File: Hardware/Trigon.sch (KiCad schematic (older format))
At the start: 110 parts, among them J1 TYPE-C-31-M12_13, J2 TYPE-C-31-M12_13, J3 Conn_01x05, SW1 SW_Push, SW2 Rotary_Encoder_Switch, U1 ATmega32U4-AU, U2 USBLC6-2SC6, U3 CY7C65632-28LTXCT, U4 USBLC6-2SC6, Y1 16MHz, Y2 12MHz

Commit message: crystal load
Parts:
- C12, C13, C14, C17, C18, C21, C4, C5, C6, C8: Manufacturer Part # CC0805KRX7R9BB104 -> CC0603KRX7R9BB104
- C19, C20: Manufacturer Part # (none) -> CC0603KRX7R9BB104
- Y1: Manufacturer Part # X322516MLB4SI -> X322516MOB4SI
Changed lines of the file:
@@
 F 2 "Capacitor_SMD:C_0603_1608Metric" H 4700 3200 50  0001 C CNN
 F 3 "~" H 4700 3200 50  0001 C CNN
-F 4 "CC0805KRX7R9BB104" H 4700 3200 50  0001 C CNN "Manufacturer Part #"
+F 4 "CC0603KRX7R9BB104" H 4700 3200 50  0001 C CNN "Manufacturer Part #"
 	1    4700 3200
 	1    0    0    -1
@@
 F 2 "Capacitor_SMD:C_0603_1608Metric" H 5000 3200 50  0001 C CNN
 F 3 "~" H 5000 3200 50  0001 C CNN
-F 4 "CC0805KRX7R9BB104" H 5000 3200 50  0001 C CNN "Manufacturer Part #"
+F 4 "CC0603KRX7R9BB104" H 5000 3200 50  0001 C CNN "Manufacturer Part #"
 	1    5000 3200
 	1    0    0    -1
@@
 F 2 "Capacitor_SMD:C_0603_1608Metric" H 5300 3200 50  0001 C CNN
 F 3 "~" H 5300 3200 50  0001 C CNN
-F 4 "CC0805KRX7R9BB104" H 5300 3200 50  0001 C CNN "Manufacturer Part #"
+F 4 "CC0603KRX7R9BB104" H 5300 3200 50  0001 C CNN "Manufacturer Part #"
 	1    5300 3200
 	1    0    0    -1
@@
 F 2 "Capacitor_SMD:C_0603_1608Metric" H 10450 13900 50  0001 C CNN
 F 3 "~" H 10450 13900 50  0001 C CNN
-F 4 "CC0805KRX7R9BB104" H 10450 13900 50  0001 C CNN "Manufacturer Part #"
+F 4 "CC0603KRX7R9BB104" H 10450 13900 50  0001 C CNN "Manufacturer Part #"
 	1    10450 13900
 	1    0    0    -1
@@
 F 2 "Capacitor_SMD:C_0603_1608Metric" H 11500 13800 50  0001 C CNN
 F 3 "~" H 11500 13800 50  0001 C CNN
-F 4 "CC0805KRX7R9BB104" H 11500 13800 50  0001 C CNN "Manufacturer Part #"
+F 4 "CC0603KRX7R9BB104" H 11500 13800 50  0001 C CNN "Manufacturer Part #"
 	1    11500 13800
 	1    0    0    -1
@@
 F 2 "Capacitor_SMD:C_0603_1608Metric" H 11950 13800 50  0001 C CNN
 F 3 "~" H 11950 13800 50  0001 C CNN
-F 4 "CC0805KRX7R9BB104" H 11950 13800 50  0001 C CNN "Manufacturer Part #"
+F 4 "CC0603KRX7R9BB104" H 11950 13800 50  0001 C CNN "Manufacturer Part #"
 	1    11950 13800
 	1    0    0    -1
@@
 F 2 "Capacitor_SMD:C_0603_1608Metric" H 13300 13800 50  0001 C CNN
 F 3 "~" H 13300 13800 50  0001 C CNN
-F 4 "CC0805KRX7R9BB104" H 13300 13800 50  0001 C CNN "Manufacturer Part #"
+F 4 "CC0603KRX7R9BB104" H 13300 13800 50  0001 C CNN "Manufacturer Part #"
 	1    13300 13800
 	1    0    0    -1
@@
 F 2 "Capacitor_SMD:C_0603_1608Metric" H 8350 10200 50  0001 C CNN
 F 3 "~" H 8350 10200 50  0001 C CNN
-F 4 "CC0805KRX7R9BB104" H 8350 10200 50  0001 C CNN "Manufacturer Part #"
+F 4 "CC0603KRX7R9BB104" H 8350 10200 50  0001 C CNN "Manufacturer Part #"
 	1    8350 10200
 	1    0    0    -1
@@
 F 2 "Capacitor_SMD:C_0603_1608Metric" H 19750 7350 50  0001 C CNN
 F 3 "~" H 19750 7350 50  0001 C CNN
-F 4 "CC0805KRX7R9BB104" H 19750 7350 50  0001 C CNN "Manufacturer Part #"
+F 4 "CC0603KRX7R9BB104" H 19750 7350 50  0001 C CNN "Manufacturer Part #"
 	1    19750 7350
 	1    0    0    -1
@@
 F 2 "Crystal:Crystal_SMD_3225-4Pin_3.2x2.5mm" H 1750 2350 50  0001 C CNN
 F 3 "~" H 1750 2350 50  0001 C CNN
-F 4 "X322516MLB4SI" H 1750 2350 50  0001 C CNN "Manufacturer Part #"
+F 4 "X322516MOB4SI" H 1750 2350 50  0001 C CNN "Manufacturer Part #"
 	1    1750 2350
 	0    1    1    0
@@
 F 2 "Capacitor_SMD:C_0603_1608Metric" H 1500 10400 50  0001 C CNN
 F 3 "~" H 1500 10400 50  0001 C CNN
+F 4 "CC0603KRX7R9BB104" H 1500 10400 50  0001 C CNN "Manufacturer Part #"
 	1    1500 10400
 	1    0    0    -1
@@
 F 2 "Capacitor_SMD:C_0603_1608Metric" H 18300 10350 50  0001 C CNN
 F 3 "~" H 18300 10350 50  0001 C CNN
+F 4 "CC0603KRX7R9BB104" H 18300 10350 50  0001 C CNN "Manufacturer Part #"
 	1    18300 10350
 	1    0    0    -1
@@
 F 2 "Capacitor_SMD:C_0603_1608Metric" H 3300 7450 50  0001 C CNN
 F 3 "~" H 3300 7450 50  0001 C CNN
-F 4 "CC0805KRX7R9BB104" H 3300 7450 50  0001 C CNN "Manufacturer Part #"
+F 4 "CC0603KRX7R9BB104" H 3300 7450 50  0001 C CNN "Manufacturer Part #"
 	1    3300 7450
 	1    0    0    -1

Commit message: Gerbers
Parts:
- J3: Manufacturer Part # (none) -> SM05B-SRSS-TB(LF)(SN)
- R15, R16: Manufacturer Part # (none) -> 0603WAF1003T5E
- U2, U4: Manufacturer Part # (none) -> USBLC6-2SC6
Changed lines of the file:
@@
 F 2 "Resistor_SMD:R_0603_1608Metric" H 1250 10400 50  0001 C CNN
 F 3 "~" H 1250 10400 50  0001 C CNN
+F 4 "0603WAF1003T5E" H 1250 10400 50  0001 C CNN "Manufacturer Part #"
 	1    1250 10400
 	1    0    0    -1
@@
 F 2 "Resistor_SMD:R_0603_1608Metric" H 18050 10350 50  0001 C CNN
 F 3 "~" H 18050 10350 50  0001 C CNN
+F 4 "0603WAF1003T5E" H 18050 10350 50  0001 C CNN "Manufacturer Part #"
 	1    18050 10350
 	1    0    0    -1
@@
 F 2 "Package_TO_SOT_SMD:SOT-23-6" H 2850 9650 50  0001 C CNN
 F 3 "http://www2.st.com/resource/en/datasheet/CD00050750.pdf" H 3800 9600 50  0001 C CNN
+F 4 "USBLC6-2SC6" H 3600 9250 50  0001 C CNN "Manufacturer Part #"
 	1    3600 9250
 	1    0    0    -1
@@
 F 2 "Package_TO_SOT_SMD:SOT-23-6" H 20150 9550 50  0001 C CNN
 F 3 "http://www2.st.com/resource/en/datasheet/CD00050750.pdf" H 21100 9500 50  0001 C CNN
+F 4 "USBLC6-2SC6" H 20900 9150 50  0001 C CNN "Manufacturer Part #"
 	1    20900 9150
 	1    0    0    -1
@@
 F 2 "Connector_JST:JST_SH_SM05B-SRSS-TB_1x05-1MP_P1.00mm_Horizontal" H 19650 12900 50  0001 C CNN
 F 3 "~" H 19650 12900 50  0001 C CNN
+F 4 "SM05B-SRSS-TB(LF)(SN)" H 19650 12900 50  0001 C CNN "Manufacturer Part #"
 	1    19650 12900
 	1    0    0    -1

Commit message: New layout
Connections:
- net +3V3: now also FB1.1, U3.21 (VCC_D); no longer C8.1, FB1.2
- new net: C8.1, FB1.2
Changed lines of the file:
@@
 Text GLabel 9400 13650 0    50   Input ~ 0
 VREG_3V3
-$Comp
-L power:+3.3V #PWR0132
-U 1 1 5F992A63
-P 9850 13550
-F 0 "#PWR0132" H 9850 13400 50  0001 C CNN
-F 1 "+3.3V" H 9865 13723 50  0000 C CNN
-F 2 "" H 9850 13550 50  0001 C CNN
-F 3 "" H 9850 13550 50  0001 C CNN
-	1    9850 13550
-	1    0    0    -1
-$EndComp
 Wire Wire Line
 	9400 13650 9650 13650
-Wire Wire Line
-	9850 13650 9850 13550
 $Comp
 L Device:C_Small C12
@@
 $EndComp
 Wire Wire Line
-	9850 13650 10050 13650
-Connection ~ 9850 13650
+	9650 13650 10050 13650
 $Comp
 L power:+3.3VA #PWR0133
@@
 	9650 13800 9650 13650
 Connection ~ 9650 13650
-Wire Wire Line
-	9650 13650 9850 13650
 $Comp
 L power:GND #PWR0134
@@
 $EndComp
 Wire Wire Line
-	8350 10100 8350 10050
-Wire Wire Line
 	8350 10300 8350 10400
 NoConn ~ 19200 7600
@@
 Wire Wire Line
 	2300 2800 2300 2850
-$Comp
-L power:+3.3V #PWR0122
-U 1 1 5F430011
-P 8250 10050
-F 0 "#PWR0122" H 8250 9900 50  0001 C CNN
-F 1 "+3.3V" V 8265 10178 50  0000 L CNN
-F 2 "" H 8250 10050 50  0001 C CNN
-F 3 "" H 8250 10050 50  0001 C CNN
-	1    8250 10050
-	0    -1   -1   0
-$EndComp
-Wire Wire Line
-	8250 10050 8350 10050
-Wire Wire Line
-	10150 9750 10850 9750
+Wire Wire Line
+	10150 9750 10350 9750
 Wire Wire Line
 	9950 9750 8350 9750
-Wire Wire Line
-	8350 9750 8350 10050
-Connection ~ 8350 10050
 Wire Wire Line
 	3800 7250 4200 7250
@@
 	1    0    0    -1
 $EndComp
+Wire Wire Line
+	8350 9750 8350 10100
+Wire Wire Line
+	10350 9700 10350 9750
+Connection ~ 10350 9750
+Wire Wire Line
+	10350 9750 10850 9750
+Wire Wire Line
+	9650 13450 9650 13650
+$Comp
+L power:+3.3V #PWR?
+U 1 1 5F5BCA3D
+P 9650 13450
+F 0 "#PWR?" H 9650 13300 50  0001 C CNN
+F 1 "+3.3V" H 9665 13623 50  0000 C CNN
+F 2 "" H 9650 13450 50  0001 C CNN
+F 3 "" H 9650 13450 50  0001 C CNN
+	1    9650 13450
+	1    0    0    -1
+$EndComp
+$Comp
+L power:+3.3V #PWR?
+U 1 1 5F5BDDAA
+P 10350 9700
+F 0 "#PWR?" H 10350 9550 50  0001 C CNN
+F 1 "+3.3V" H 10365 9873 50  0000 C CNN
+F 2 "" H 10350 9700 50  0001 C CNN
+F 3 "" H 10350 9700 50  0001 C CNN
+	1    10350 9700
+	1    0    0    -1
+$EndComp

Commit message: Latest bom/gerbers; reflecting more of josh's comments
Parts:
- R10: Manufacturer Part # 0603WAF6500T5E -> 0603WAF6490T5E
- Y1: Manufacturer Part # X322516MOB4SI -> X322516MRB4SI
- Y2: Manufacturer Part # X322512MOB4SI -> X322512MSB4SI
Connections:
- net D2_D+: now also J3.5 (Pin_5); no longer J3.1 (Pin_1)
- net D2_D-: now also J3.4 (Pin_4); no longer J3.2 (Pin_2)
- net GND: now also J3.1 (Pin_1); no longer J3.5 (Pin_5)
- no-connect marks 22 -> 23
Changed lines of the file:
@@
 Wire Wire Line
 	10550 10850 10850 10850
-$Comp
-L power:+3.3V #PWR0126
-U 1 1 5F75C131
-P 10250 10750
-F 0 "#PWR0126" H 10250 10600 50  0001 C CNN
-F 1 "+3.3V" H 10265 10923 50  0000 C CNN
-F 2 "" H 10250 10750 50  0001 C CNN
-F 3 "" H 10250 10750 50  0001 C CNN
-	1    10250 10750
-	1    0    0    -1
-$EndComp
-Wire Wire Line
-	10550 10750 10250 10750
 Wire Wire Line
 	10350 10850 10250 10850
-Wire Wire Line
-	10250 10850 10250 10750
-Connection ~ 10250 10750
 $Comp
 L Device:R_Small R8
@@
 F 2 "Resistor_SMD:R_0603_1608Metric" H 10800 11300 50  0001 C CNN
 F 3 "~" H 10800 11300 50  0001 C CNN
-F 4 "0603WAF6500T5E" H 10800 11300 50  0001 C CNN "Manufacturer Part #"
+F 4 "0603WAF6490T5E" H 10800 11300 50  0001 C CNN "Manufacturer Part #"
 	1    10800 11300
 	1    0    0    -1
@@
 F 2 "Crystal:Crystal_SMD_3225-4Pin_3.2x2.5mm" H 9750 10300 50  0001 C CNN
 F 3 "~" H 9750 10300 50  0001 C CNN
-F 4 "X322512MOB4SI" H 9750 10300 50  0001 C CNN "Manufacturer Part #"
+F 4 "X322512MSB4SI" H 9750 10300 50  0001 C CNN "Manufacturer Part #"
 	1    9750 10300
 	0    1    1    0
@@
 F 2 "Crystal:Crystal_SMD_3225-4Pin_3.2x2.5mm" H 1750 2350 50  0001 C CNN
 F 3 "~" H 1750 2350 50  0001 C CNN
-F 4 "X322516MOB4SI" H 1750 2350 50  0001 C CNN "Manufacturer Part #"
+F 4 "X322516MRB4SI" H 1750 2350 50  0001 C CNN "Manufacturer Part #"
 	1    1750 2350
 	0    1    1    0
@@
 L power:GND #PWR0142
 U 1 1 5F449573
-P 19150 13350
-F 0 "#PWR0142" H 19150 13100 50  0001 C CNN
-F 1 "GND" H 19155 13177 50  0000 C CNN
-F 2 "" H 19150 13350 50  0001 C CNN
-F 3 "" H 19150 13350 50  0001 C CNN
-	1    19150 13350
-	1    0    0    -1
-$EndComp
-Wire Wire Line
-	19450 13100 19150 13100
-Wire Wire Line
-	19150 13100 19150 13350
-Text GLabel 19450 12800 0    50   Output ~ 0
+P 19250 12300
+F 0 "#PWR0142" H 19250 12050 50  0001 C CNN
+F 1 "GND" H 19255 12127 50  0000 C CNN
+F 2 "" H 19250 12300 50  0001 C CNN
+F 3 "" H 19250 12300 50  0001 C CNN
+	1    19250 12300
+	1    0    0    -1
+$EndComp
+Text GLabel 19450 13000 0    50   Output ~ 0
 D2_D-
-Text GLabel 19450 12700 0    50   Output ~ 0
+Text GLabel 19450 13100 0    50   Output ~ 0
 D2_D+
 Wire Wire Line
 	19450 12900 18850 12900
-NoConn ~ 19450 13000
 NoConn ~ 11850 9750
 NoConn ~ 11850 9850
@@
 	9650 13450 9650 13650
 $Comp
-L power:+3.3V #PWR?
+L power:+3.3V #PWR0122
 U 1 1 5F5BCA3D
 P 9650 13450
-F 0 "#PWR?" H 9650 13300 50  0001 C CNN
+F 0 "#PWR0122" H 9650 13300 50  0001 C CNN
 F 1 "+3.3V" H 9665 13623 50  0000 C CNN
 F 2 "" H 9650 13450 50  0001 C CNN
@@
 $EndComp
 $Comp
-L power:+3.3V #PWR?
+L power:+3.3V #PWR0132
 U 1 1 5F5BDDAA
 P 10350 9700
-F 0 "#PWR?" H 10350 9550 50  0001 C CNN
+F 0 "#PWR0132" H 10350 9550 50  0001 C CNN
 F 1 "+3.3V" H 10365 9873 50  0000 C CNN
 F 2 "" H 10350 9700 50  0001 C CNN
@@
 	1    0    0    -1
 $EndComp
+Connection ~ 10250 10750
+Wire Wire Line
+	10250 10850 10250 10750
+Wire Wire Line
+	10550 10750 10250 10750
+$Comp
+L power:+3.3V #PWR0126
+U 1 1 5F75C131
+P 10250 10750
+F 0 "#PWR0126" H 10250 10600 50  0001 C CNN
+F 1 "+3.3V" H 10265 10923 50  0000 C CNN
+F 2 "" H 10250 10750 50  0001 C CNN
+F 3 "" H 10250 10750 50  0001 C CNN
+	1    10250 10750
+	1    0    0    -1
+$EndComp
+Wire Wire Line
+	19450 12700 19450 12300
+Wire Wire Line
+	19450 12300 19250 12300
+NoConn ~ 19450 12800
+NoConn ~ 13150 12200
 $EndSCHEMATC

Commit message: Checkin
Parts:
- C1, C10, C2, C9: Manufacturer Part # CL21C220JBANNNC -> CL10C220JB8NNNC
- C11, C7: Manufacturer Part # CL21A106KAYNNNE -> CL10A106KP8NNNC
- C15, C16, C3: Manufacturer Part # CL21B105KBFNNNE -> CL10A105KB8NNNC
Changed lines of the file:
@@
 F 2 "Capacitor_SMD:C_0603_1608Metric" H 1950 3450 50  0001 C CNN
 F 3 "~" H 1950 3450 50  0001 C CNN
-F 4 "CL21B105KBFNNNE" H 1950 3450 50  0001 C CNN "Manufacturer Part #"
+F 4 "CL10A105KB8NNNC" H 1950 3450 50  0001 C CNN "Manufacturer Part #"
 	1    1950 3450
 	1    0    0    -1
@@
 F 2 "Capacitor_SMD:C_0603_1608Metric" H 5650 3200 50  0001 C CNN
 F 3 "~" H 5650 3200 50  0001 C CNN
-F 4 "CL21A106KAYNNNE" H 5650 3200 50  0001 C CNN "Manufacturer Part #"
+F 4 "CL10A106KP8NNNC" H 5650 3200 50  0001 C CNN "Manufacturer Part #"
 	1    5650 3200
 	1    0    0    -1
@@
 F 2 "Capacitor_SMD:C_0603_1608Metric" H 1350 2500 50  0001 C CNN
 F 3 "~" H 1350 2500 50  0001 C CNN
-F 4 "CL21C220JBANNNC" H 1350 2500 50  0001 C CNN "Manufacturer Part #"
+F 4 "CL10C220JB8NNNC" H 1350 2500 50  0001 C CNN "Manufacturer Part #"
 	1    1350 2500
 	0    1    1    0
@@
 F 2 "Capacitor_SMD:C_0603_1608Metric" H 1350 2150 50  0001 C CNN
 F 3 "~" H 1350 2150 50  0001 C CNN
-F 4 "CL21C220JBANNNC" H 1350 2150 50  0001 C CNN "Manufacturer Part #"
+F 4 "CL10C220JB8NNNC" H 1350 2150 50  0001 C CNN "Manufacturer Part #"
 	1    1350 2150
 	0    1    1    0
@@
 F 2 "Capacitor_SMD:C_0603_1608Metric" H 9350 10450 50  0001 C CNN
 F 3 "~" H 9350 10450 50  0001 C CNN
-F 4 "CL21C220JBANNNC" H 9350 10450 50  0001 C CNN "Manufacturer Part #"
+F 4 "CL10C220JB8NNNC" H 9350 10450 50  0001 C CNN "Manufacturer Part #"
 	1    9350 10450
 	0    1    1    0
@@
 F 2 "Capacitor_SMD:C_0603_1608Metric" H 9350 10100 50  0001 C CNN
 F 3 "~" H 9350 10100 50  0001 C CNN
-F 4 "CL21C220JBANNNC" H 9350 10100 50  0001 C CNN "Manufacturer Part #"
+F 4 "CL10C220JB8NNNC" H 9350 10100 50  0001 C CNN "Manufacturer Part #"
 	1    9350 10100
 	0    1    1    0
@@
 F 2 "Capacitor_SMD:C_0603_1608Metric" H 12400 13800 50  0001 C CNN
 F 3 "~" H 12400 13800 50  0001 C CNN
-F 4 "CL21B105KBFNNNE" H 12400 13800 50  0001 C CNN "Manufacturer Part #"
+F 4 "CL10A105KB8NNNC" H 12400 13800 50  0001 C CNN "Manufacturer Part #"
 	1    12400 13800
 	1    0    0    -1
@@
 F 2 "Capacitor_SMD:C_0603_1608Metric" H 12850 13800 50  0001 C CNN
 F 3 "~" H 12850 13800 50  0001 C CNN
-F 4 "CL21B105KBFNNNE" H 12850 13800 50  0001 C CNN "Manufacturer Part #"
+F 4 "CL10A105KB8NNNC" H 12850 13800 50  0001 C CNN "Manufacturer Part #"
 	1    12850 13800
 	1    0    0    -1
@@
 F 2 "Capacitor_SMD:C_0603_1608Metric" H 9650 13900 50  0001 C CNN
 F 3 "~" H 9650 13900 50  0001 C CNN
-F 4 "CL21A106KAYNNNE" H 9650 13900 50  0001 C CNN "Manufacturer Part #"
+F 4 "CL10A106KP8NNNC" H 9650 13900 50  0001 C CNN "Manufacturer Part #"
 	1    9650 13900
 	1    0    0    -1

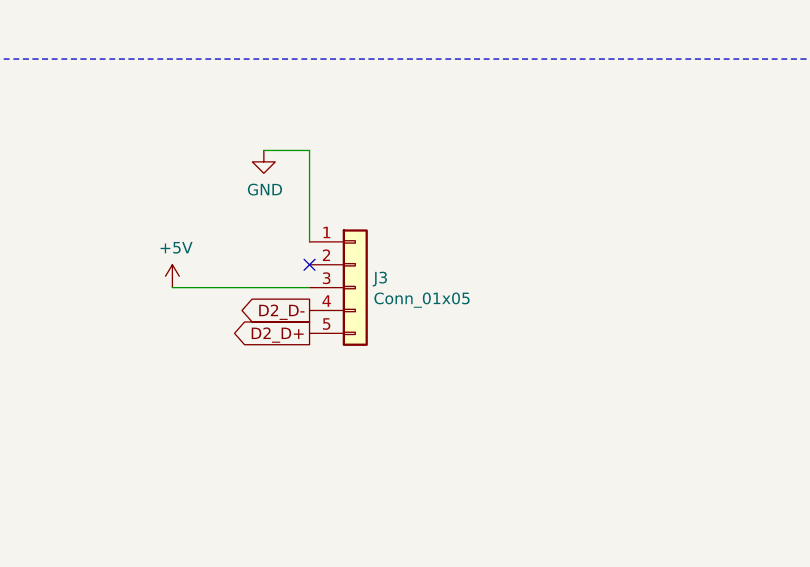
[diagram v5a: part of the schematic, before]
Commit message: Updates to case
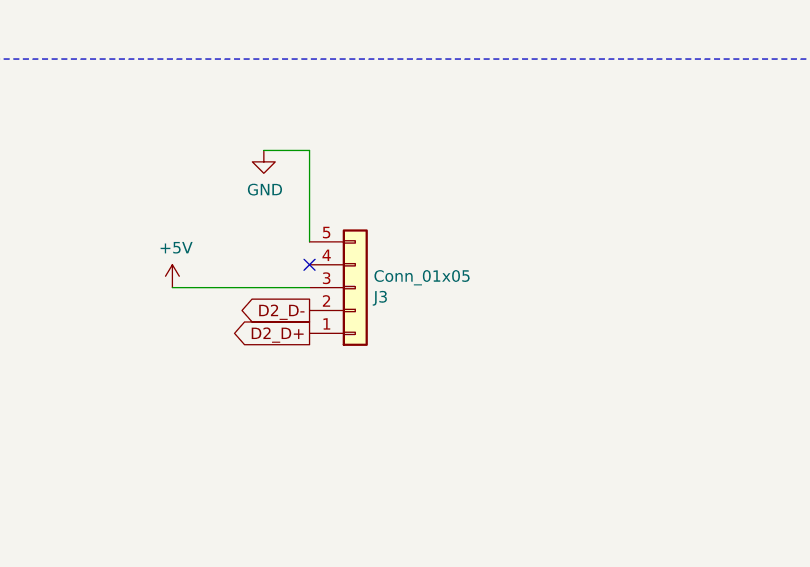
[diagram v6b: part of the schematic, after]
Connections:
- net D2_D+: now also J3.1 (Pin_1); no longer J3.5 (Pin_5)
- net D2_D-: now also J3.2 (Pin_2); no longer J3.4 (Pin_4)
- net GND: now also J3.5 (Pin_5); no longer J3.1 (Pin_1)
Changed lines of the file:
@@
 F 4 "SM05B-SRSS-TB(LF)(SN)" H 19650 12900 50  0001 C CNN "Manufacturer Part #"
 	1    19650 12900
-	1    0    0    -1
+	1    0    0    1
 $EndComp
 $Comp
